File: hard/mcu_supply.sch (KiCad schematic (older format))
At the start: 20 parts

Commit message: attribute naming update
JLCPCB_Part_Number -> LCSC
DigiKey_Part_Number -> DigiKey
Mouser_Part_Number -> Mouser
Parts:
- MCU?: JLCPCB_Part_Number C91929 -> (none); LCSC (none) -> C91929
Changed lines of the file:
@@
 F 2 "led_matrix:LQFP-100_14x14mm_P0.5mm" H 6750 1750 50  0001 C CNN
 F 3 "https://www.st.com/resource/en/datasheet/stm32f446ve.pdf" H 6750 1750 50  0001 C CNN
-F 4 "C91929" H 6200 1400 50  0001 C CNN "JLCPCB_Part_Number"
+F 4 "C91929" H 6200 1400 50  0001 C CNN "LCSC"
 F 5 "STMicroelectronics" H 6200 1400 50  0001 C CNN "MF"
 F 6 "STM32F446VET6" H 6200 1400 50  0001 C CNN "MPN"

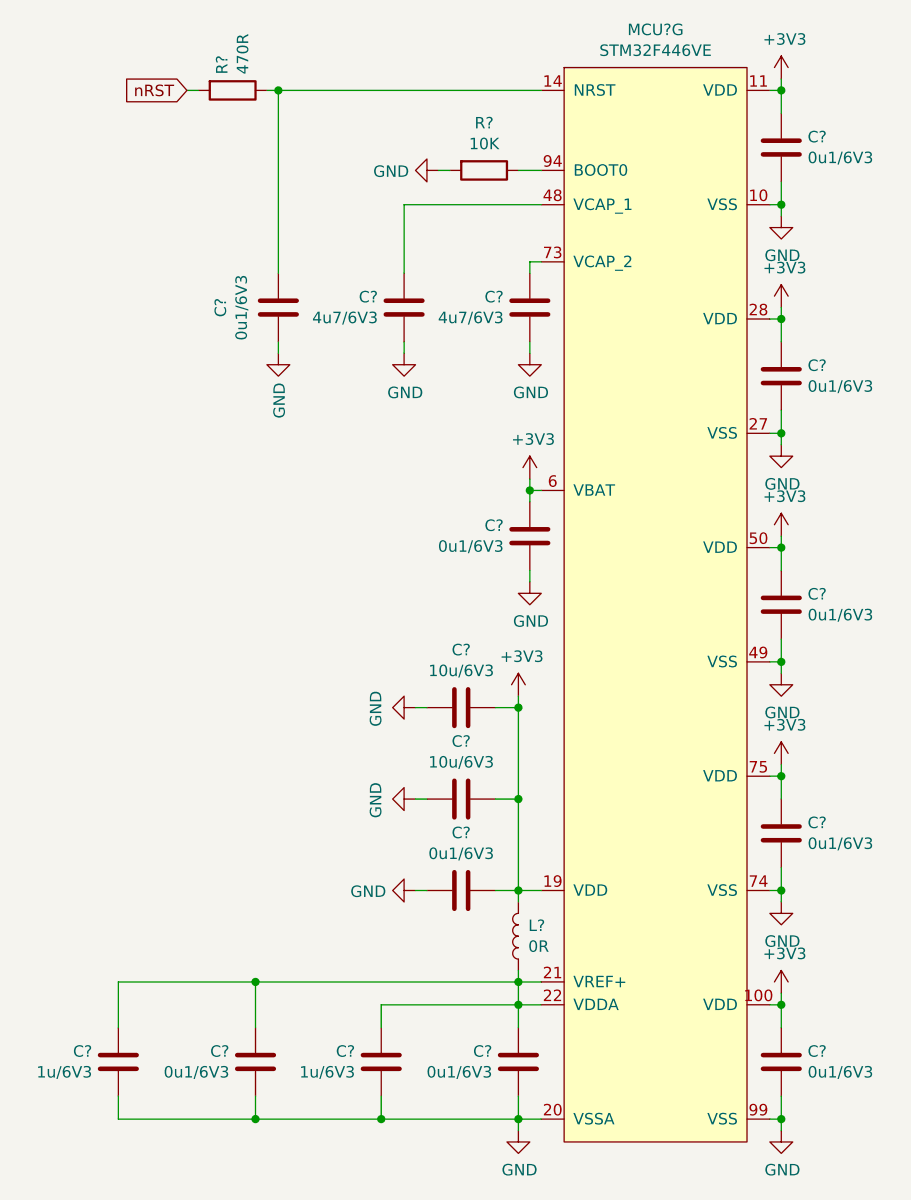
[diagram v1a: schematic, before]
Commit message: re-connect footprints
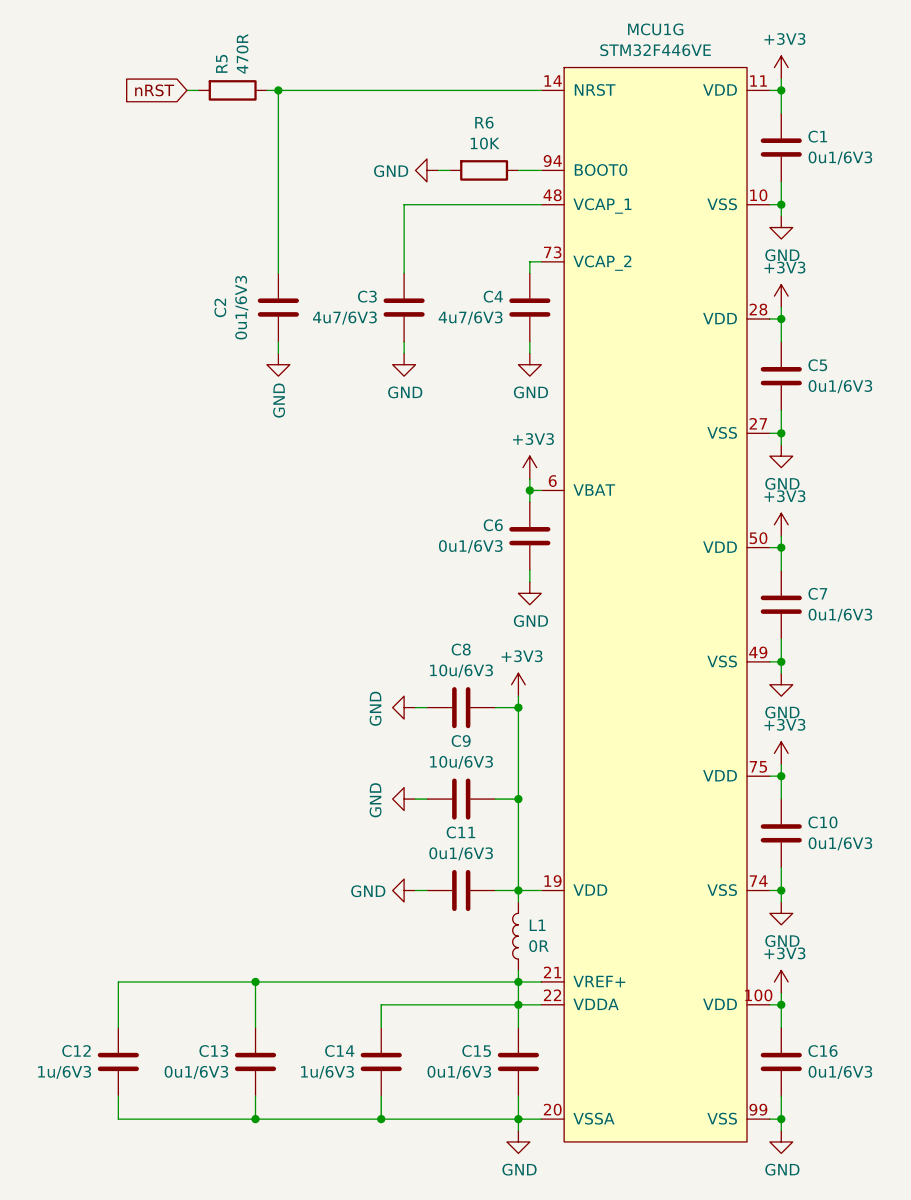
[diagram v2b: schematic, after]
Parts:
- gave numbers to parts that had none: 20
